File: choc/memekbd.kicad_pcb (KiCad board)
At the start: 2 copper layers, 3.6 x 3.1 mm, 192 parts, among them J1 USB_B_Micro, J2 USB_B_Micro, SW1 SW_Push, SW10 SW_Push, SW11 SW_Push, SW12 SW_Push, SW13 SW_Push, SW14 SW_Push, SW15 SW_Push, SW16 SW_Push, SW17 SW_Push, SW18 SW_Push, SW19 SW_Push, SW2 SW_Push, SW20 SW_Push, SW21 SW_Push, SW22 SW_Push, SW23 SW_Push, SW24 SW_Push, SW25 SW_Push, SW26 SW_Push, SW27 SW_Push, SW28 SW_Push, SW29 SW_Push, SW3 SW_Push, SW30 SW_Push, SW31 SW_Push, SW32 SW_Push, SW33 SW_Push, SW34 SW_Push, SW35 SW_Push, SW36 SW_Push, SW37 SW_Push, SW38 SW_Push, SW39 SW_Push, SW4 SW_Push, SW40 SW_Push, SW41 SW_Push, SW42 SW_Push, SW43 SW_Push, SW44 SW_Push, SW45 SW_Push, SW46 SW_Push, SW47 SW_Push, SW48 SW_Push, SW49 SW_Push, SW5 SW_Push, SW50 SW_Push, SW6 SW_Push, SW7 SW_Push, SW8 SW_Push, SW9 SW_Push, U1 ProMicro, U2 ProMicro

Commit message: work on choc version
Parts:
- moved H4 193.7 mm to (96.0, 21.8)
- moved H6 189.2 mm to (111.8, 96.5)
- moved H7 157.7 mm to (74.8, 96.5)
- moved H5 143.8 mm to (74.0, 21.8)
- moved H3 100.1 mm to (46.8, 73.5)
- moved C1 83.9 mm to (80.0, 104.5)
- moved C11 83.9 mm to (104.0, 104.5)
- moved C12 83.9 mm to (107.0, 104.5)
- moved C2 83.9 mm to (83.0, 104.5)
- moved C3 83.9 mm to (86.0, 104.5)
- moved C4 83.9 mm to (89.0, 104.5)
- moved C6 83.9 mm to (92.0, 104.5)
- moved C7 83.9 mm to (95.0, 104.5)
- moved C8 83.9 mm to (98.0, 104.5)
- moved C9 83.9 mm to (101.0, 104.5)
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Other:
- board size 3.6 x 3.1 mm -> 260 x 92.5 mm

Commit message: add mounting holes
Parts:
- moved H16 137.7 mm to (243.0, 73.2)
- moved H12 124.8 mm to (195.5, 21.5)
- moved H9 122.8 mm to (217.0, 21.5)
- moved H11 114.9 mm to (180.0, 96.0)
- moved H15 112.6 mm to (265.2, 28.5)
- moved H14 106.5 mm to (217.0, 96.0)
- moved H13 100.8 mm to (235.0, 89.2)
- moved H10 88.4 mm to (272.8, 87.8)
- moved H2 5.76 mm to (19.2, 88.2)
- moved H1 5.75 mm to (56.0, 89.8)
- moved C13 3.44 mm to (183.6, 106.2)
- moved C14 3.44 mm to (186.6, 106.2)
- moved C16 3.44 mm to (189.6, 106.2)
- moved C17 3.44 mm to (192.6, 106.2)
- moved C18 3.44 mm to (195.6, 106.2)
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
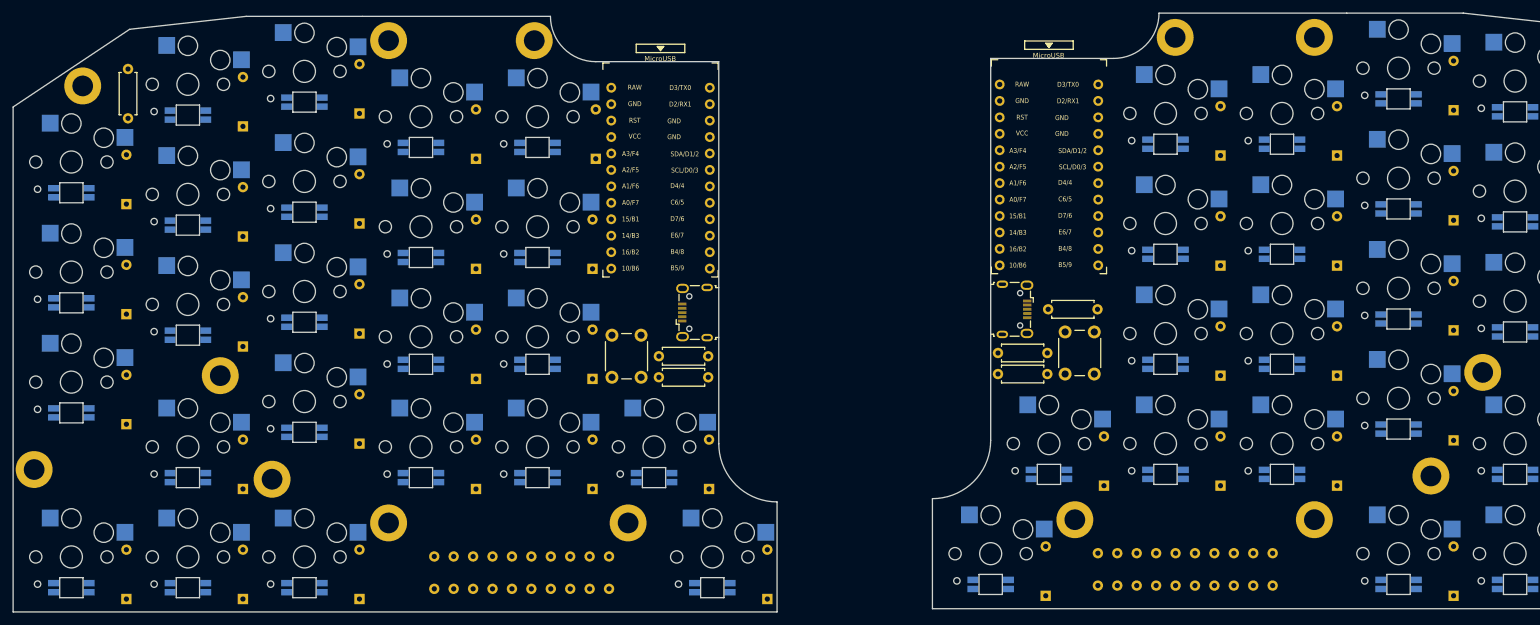
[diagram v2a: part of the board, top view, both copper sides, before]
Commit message: fix diodes not having vertical space in choc
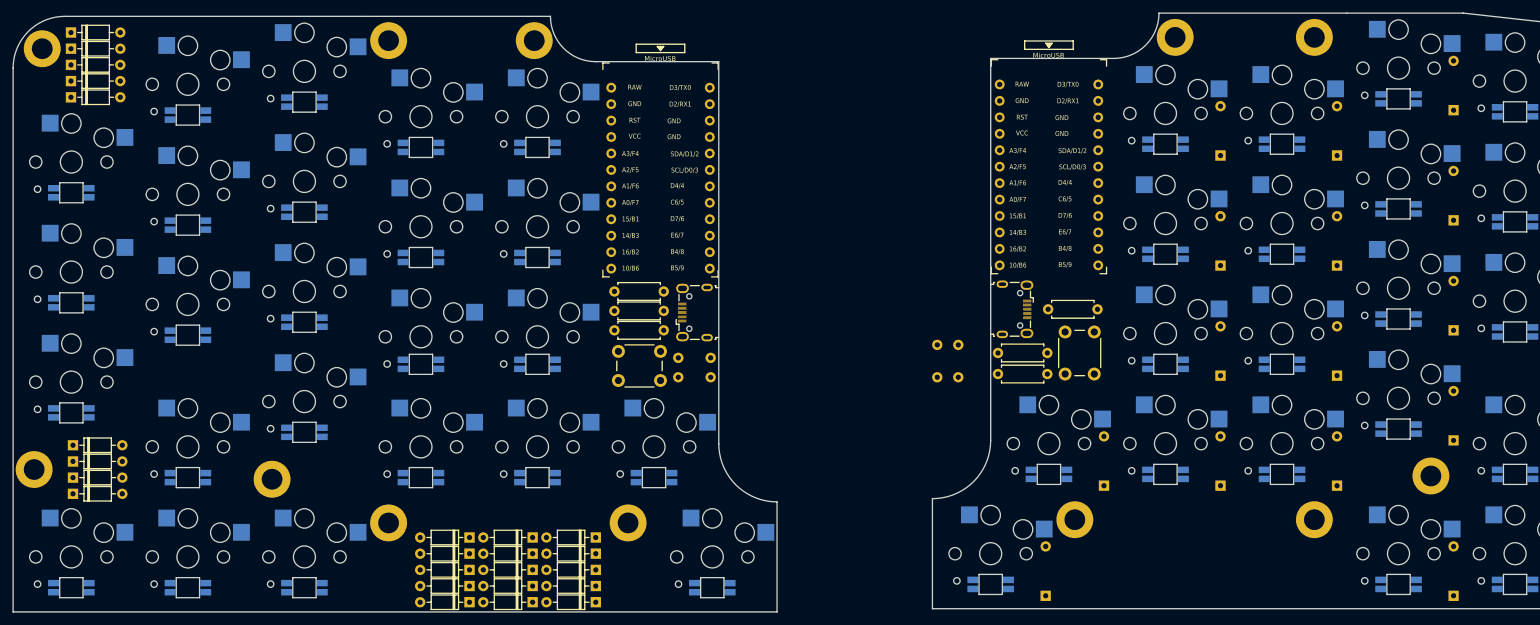
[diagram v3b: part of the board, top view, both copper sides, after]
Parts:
- removed C11, C12, C13, C14, C16, C17, C18, C19, C20, C21, C22, C23, C6, C7, C8, C9: 0.1uF, Capacitor_THT:C_Disc_D6.0mm_W2.5mm_P5.00mm
- removed H16, H3: MountingHole_Pad, MountingHole:MountingHole_3.2mm_M3_ISO7380_Pad
- D1, D10, D11, D12, D13, D14, D15, D16, D17, D18, D19, D2, D20, D21, D22, D23, D3, D4, D47, D5, D6, D7, D8, D9: moved to F.Cu
- moved R5 87.0 mm to (116.5, 60.8), turned to 180 degrees
- moved D20 83.4 mm to (24.9, 20.8), turned to 0 degrees
- moved C4 79.0 mm to (162.0, 74.0)
- moved C3 78.8 mm to (158.8, 74.0)
- moved D2 69.2 mm to (86.5, 108.8), turned to 180 degrees
- moved D3 68.5 mm to (96.2, 108.8), turned to 180 degrees
- moved D7 64.4 mm to (86.5, 106.2), turned to 180 degrees
- moved D16 63.3 mm to (24.9, 30.8), turned to 0 degrees
- moved D8 58.1 mm to (96.2, 106.2), turned to 180 degrees
- moved D12 56.1 mm to (86.5, 103.8), turned to 180 degrees
- moved C1 51.9 mm to (118.8, 71.0), turned to 0 degrees
- moved C2 47.7 mm to (118.8, 74.0), turned to 0 degrees
- moved D47 47.1 mm to (25.2, 92.0), turned to 0 degrees
- moved D21 45.6 mm to (86.5, 98.8), turned to 180 degrees
- moved D13 45.3 mm to (96.2, 103.8), turned to 180 degrees
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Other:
- outline, holes or cut-outs redrawn

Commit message: progress
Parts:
- moved H15 8.49 mm to (271.2, 22.5)
- moved H8 0.35 mm to (20.8, 23.0)
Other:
- outline, holes or cut-outs redrawn
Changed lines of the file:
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@@
     (pad "" np_thru_hole circle (at 5.5 0 180) (size 1.9 1.9) (drill 1.9) (layers F&B.Cu *.Mask))
     (pad "1" smd rect (at 3.275 6 180) (size 2.6 2.6) (layers "B.Cu" "B.Paste" "B.Mask")
-      (net 111 "/lcol4") (pinfunction "1") (pintype "passive"))
+      (net 111 "/lcol4") (pinfunction "1"))
     (pad "2" smd rect (at -8.275 3.8 180) (size 2.6 2.6) (layers "B.Cu" "B.Paste" "B.Mask")
-      (net 30 "Net-(D23-Pad2)") (pinfunction "2") (pintype "passive"))
+      (net 30 "Net-(D23-Pad2)") (pinfunction "2"))
   )
   (footprint "kbd:ChocV1_Hotswap" (layer "F.Cu")
@@
   )
   (footprint "MountingHole:MountingHole_3.2mm_M3_ISO7380_Pad" (layer "F.Cu")
-    (at 265.25 28.5)
+    (at 271.25 22.5)
     (descr "Mounting Hole 3.2mm, M3, ISO7380")
     (tags "mounting hole 3.2mm m3 iso7380")
@@
   )
   (footprint "MountingHole:MountingHole_3.2mm_M3_ISO7380_Pad" (layer "F.Cu")
-    (at 20.5 23.25)
+    (at 20.75 23)
     (descr "Mounting Hole 3.2mm, M3, ISO7380")
     (tags "mounting hole 3.2mm m3 iso7380")
@@
     )
   )
-  (gr_line (start 167 24.75) (end 167 83.75) (layer "Edge.Cuts") (width 0.05))
-  (gr_line (start 276 109.75) (end 276 31.75) (layer "Edge.Cuts") (width 0.05))
+  (gr_line (start 276 109.75) (end 276 25.75) (layer "Edge.Cuts") (width 0.05))
+  (gr_line (start 186 24.75) (end 167 24.75) (layer "Edge.Cuts") (width 0.05))
   (gr_arc (start 24 26.25) (end 16 26.25) (angle 90) (layer "Edge.Cuts") (width 0.05))
-  (gr_line (start 106 25.25) (end 125 25.25) (layer "Edge.Cuts") (width 0.05))
-  (gr_arc (start 134 84.25) (end 125 84.25) (angle -90) (layer "Edge.Cuts") (width 0.05))
-  (gr_line (start 240 17.75) (end 222 17.75) (layer "Edge.Cuts") (width 0.05))
   (gr_arc (start 158 83.75) (end 167 83.75) (angle 90) (layer "Edge.Cuts") (width 0.05))
   (gr_line (start 222 17.75) (end 193 17.75) (layer "Edge.Cuts") (width 0.05))
-  (gr_line (start 276 109.75) (end 158 109.75) (layer "Edge.Cuts") (width 0.05))
-  (gr_line (start 276 31.75) (end 258 19.75) (layer "Edge.Cuts") (width 0.05))
-  (gr_line (start 258 19.75) (end 240 17.75) (layer "Edge.Cuts") (width 0.05))
-  (gr_line (start 16 110.25) (end 134 110.25) (layer "Edge.Cuts") (width 0.05))
+  (gr_line (start 106 25.25) (end 125 25.25) (layer "Edge.Cuts") (width 0.05))
+  (gr_arc (start 134 84.25) (end 125 84.25) (angle -90) (layer "Edge.Cuts") (width 0.05))
   (gr_line (start 158 109.75) (end 158 92.75) (layer "Edge.Cuts") (width 0.05))
+  (gr_line (start 167 24.75) (end 167 83.75) (layer "Edge.Cuts") (width 0.05))
+  (gr_line (start 268 17.75) (end 222 17.75) (layer "Edge.Cuts") (width 0.05))
+  (gr_arc (start 186 17.75) (end 186 24.75) (angle -90) (layer "Edge.Cuts") (width 0.05))
+  (gr_arc (start 268 25.75) (end 276 25.75) (angle -90) (layer "Edge.Cuts") (width 0.05))
+  (gr_line (start 16 110.25) (end 134 110.25) (layer "Edge.Cuts") (width 0.05))
   (gr_line (start 24 18.25) (end 70 18.25) (layer "Edge.Cuts") (width 0.05))
-  (gr_line (start 186 24.75) (end 167 24.75) (layer "Edge.Cuts") (width 0.05))
   (gr_line (start 70 18.25) (end 99 18.25) (layer "Edge.Cuts") (width 0.05))
   (gr_line (start 125 25.25) (end 125 84.25) (layer "Edge.Cuts") (width 0.05))
   (gr_line (start 16 110.25) (end 16 26.25) (layer "Edge.Cuts") (width 0.05))
-  (gr_arc (start 186 17.75) (end 186 24.75) (angle -90) (layer "Edge.Cuts") (width 0.05))
+  (gr_line (start 276 109.75) (end 158 109.75) (layer "Edge.Cuts") (width 0.05))
   (gr_arc (start 106 18.25) (end 106 25.25) (angle 90) (layer "Edge.Cuts") (width 0.05))
   (gr_line (start 134 110.25) (end 134 93.25) (layer "Edge.Cuts") (width 0.05))

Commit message: progress
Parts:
- D24, D25, D26, D27, D28, D29, D30, D31, D32, D33, D34, D35, D36, D37, D38, D39, D40, D41, D42, D43, D44, D45, D46, D48: moved to F.Cu
- moved D45 84.4 mm to (194.8, 108.2), turned to 0 degrees
- moved D44 82.9 mm to (204.5, 108.2), turned to 0 degrees
- moved D40 75.0 mm to (204.5, 105.8), turned to 0 degrees
- moved D41 72.0 mm to (194.8, 105.8), turned to 0 degrees
- moved D24 66.2 mm to (265.8, 20.2), turned to 180 degrees
- moved D35 63.4 mm to (204.5, 103.2), turned to 0 degrees
- moved D46 58.8 mm to (185.0, 108.2), turned to 0 degrees
- moved D36 57.0 mm to (194.8, 103.2), turned to 0 degrees
- moved D29 48.3 mm to (265.8, 22.8), turned to 180 degrees
- moved D30 46.8 mm to (204.5, 100.8), turned to 0 degrees
- moved D25 41.5 mm to (204.5, 98.2), turned to 0 degrees
- moved D42 38.5 mm to (185.0, 105.8), turned to 0 degrees
- moved D31 37.3 mm to (194.8, 100.8), turned to 0 degrees
- moved D28 36.1 mm to (265.8, 84.0), turned to 180 degrees
- moved D34 28.3 mm to (265.8, 25.2), turned to 180 degrees
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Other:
- board size 260 x 92.5 mm -> 259 x 92.5 mm

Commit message: progress on plates
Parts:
- added H1: MountingHole_Pad, MountingHole:MountingHole_3.2mm_M3_ISO7380_Pad, F.Cu at (207.0, 195.5)
- added H1: MountingHole_Pad, MountingHole:MountingHole_3.2mm_M3_ISO7380_Pad, F.Cu at (60.5, 192.5)
- added H2: MountingHole_Pad, MountingHole:MountingHole_3.2mm_M3_ISO7380_Pad, F.Cu at (24.5, 191.0)
- added H2: MountingHole_Pad, MountingHole:MountingHole_3.2mm_M3_ISO7380_Pad, F.Cu at (171.0, 194.0)
- added H4: MountingHole_Pad, MountingHole:MountingHole_3.2mm_M3_ISO7380_Pad, F.Cu at (248.2, 127.8)
- added H4: MountingHole_Pad, MountingHole:MountingHole_3.2mm_M3_ISO7380_Pad, F.Cu at (101.8, 124.8)
- added H5: MountingHole_Pad, MountingHole:MountingHole_3.2mm_M3_ISO7380_Pad, F.Cu at (225.0, 127.8)
- added H5: MountingHole_Pad, MountingHole:MountingHole_3.2mm_M3_ISO7380_Pad, F.Cu at (78.5, 124.8)
- added H6: MountingHole_Pad, MountingHole:MountingHole_3.2mm_M3_ISO7380_Pad, F.Cu at (117.0, 199.2)
- added H6: MountingHole_Pad, MountingHole:MountingHole_3.2mm_M3_ISO7380_Pad, F.Cu at (263.5, 202.2)
- added H7: MountingHole_Pad, MountingHole:MountingHole_3.2mm_M3_ISO7380_Pad, F.Cu at (78.5, 199.2)
- added H7: MountingHole_Pad, MountingHole:MountingHole_3.2mm_M3_ISO7380_Pad, F.Cu at (225.0, 202.2)
- added H8: MountingHole_Pad, MountingHole:MountingHole_3.2mm_M3_ISO7380_Pad, F.Cu at (172.5, 128.8)
- added H8: MountingHole_Pad, MountingHole:MountingHole_3.2mm_M3_ISO7380_Pad, F.Cu at (26.0, 125.8)
- added SW2: KEY_SWITCH, kbd:ChocV1_Hole, F.Cu at (176.8, 163.5)
- added SW2: KEY_SWITCH, kbd:ChocV1_Hole, F.Cu at (248.8, 139.5)
- added SW2: KEY_SWITCH, kbd:ChocV1_Hole, F.Cu at (194.8, 190.5)
- added SW2: KEY_SWITCH, kbd:ChocV1_Hole, F.Cu at (248.8, 190.5)
- added SW2: KEY_SWITCH, kbd:ChocV1_Hole, F.Cu at (176.8, 146.5)
- added SW2: KEY_SWITCH, kbd:ChocV1_Hole, F.Cu at (194.8, 168.5)
- added SW2: KEY_SWITCH, kbd:ChocV1_Hole, F.Cu at (266.8, 190.5)
- added SW2: KEY_SWITCH, kbd:ChocV1_Hole, F.Cu at (275.8, 207.5)
- added SW2: KEY_SWITCH, kbd:ChocV1_Hole, F.Cu at (194.8, 151.5)
- added SW2: KEY_SWITCH, kbd:ChocV1_Hole, F.Cu at (212.8, 149.5)
- added SW2: KEY_SWITCH, kbd:ChocV1_Hole, F.Cu at (176.8, 207.5)
- added SW2: KEY_SWITCH, kbd:ChocV1_Hole, F.Cu at (194.8, 134.5)
- added SW2: KEY_SWITCH, kbd:ChocV1_Hole, F.Cu at (194.8, 207.5)
- added SW2: KEY_SWITCH, kbd:ChocV1_Hole, F.Cu at (230.8, 139.5)
- added SW2 (x2): KEY_SWITCH, kbd:ChocV1_Hole, F.Cu at (212.8, 207.5)
- added SW2: KEY_SWITCH, kbd:ChocV1_Hole, F.Cu at (248.8, 173.5)
- added SW2: KEY_SWITCH, kbd:ChocV1_Hole, F.Cu at (212.8, 183.5)
- added SW2: KEY_SWITCH, kbd:ChocV1_Hole, F.Cu at (248.8, 156.5)
- added SW2: KEY_SWITCH, kbd:ChocV1_Hole, F.Cu at (230.8, 173.5)
- added SW2: KEY_SWITCH, kbd:ChocV1_Hole, F.Cu at (230.8, 190.5)
- added SW2: KEY_SWITCH, kbd:ChocV1_Hole, F.Cu at (212.8, 132.5)
- added SW2: KEY_SWITCH, kbd:ChocV1_Hole, F.Cu at (212.8, 166.5)
- added SW2: KEY_SWITCH, kbd:ChocV1_Hole, F.Cu at (230.8, 156.5)
- added SW2: KEY_SWITCH, kbd:ChocV1_Hole, F.Cu at (176.8, 180.5)
- moved D12 2.00 mm to (86.5, 101.8)
- moved D13 2.00 mm to (96.2, 101.8)
- moved D14 2.00 mm to (106.0, 101.8)
- moved D17 2.00 mm to (86.5, 99.2)
- moved D18 2.00 mm to (96.2, 99.2)
- moved D19 2.00 mm to (106.0, 99.2)
- moved D2 2.00 mm to (86.5, 106.8)
- moved D21 2.00 mm to (86.5, 96.8)
- moved D22 2.00 mm to (96.2, 96.8)
- moved D23 2.00 mm to (106.0, 96.8)
- moved D25 2.00 mm to (204.5, 96.2)
- moved D26 2.00 mm to (194.8, 96.2)
- moved D27 2.00 mm to (185.0, 96.2)
- moved D3 2.00 mm to (96.2, 106.8)
- moved D30 2.00 mm to (204.5, 98.8)
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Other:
- board size 259 x 92.5 mm -> 268.8 x 198.2 mm

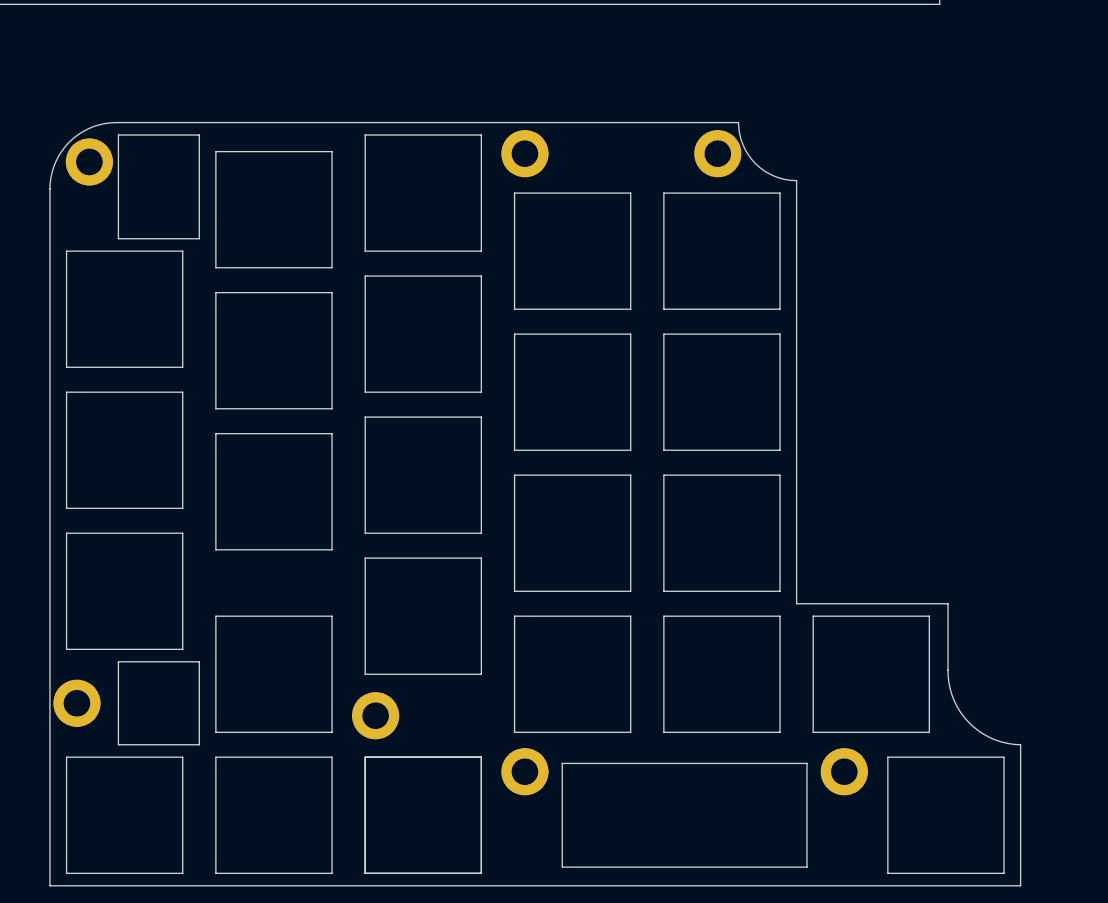
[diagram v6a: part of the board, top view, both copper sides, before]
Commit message: add routed left board
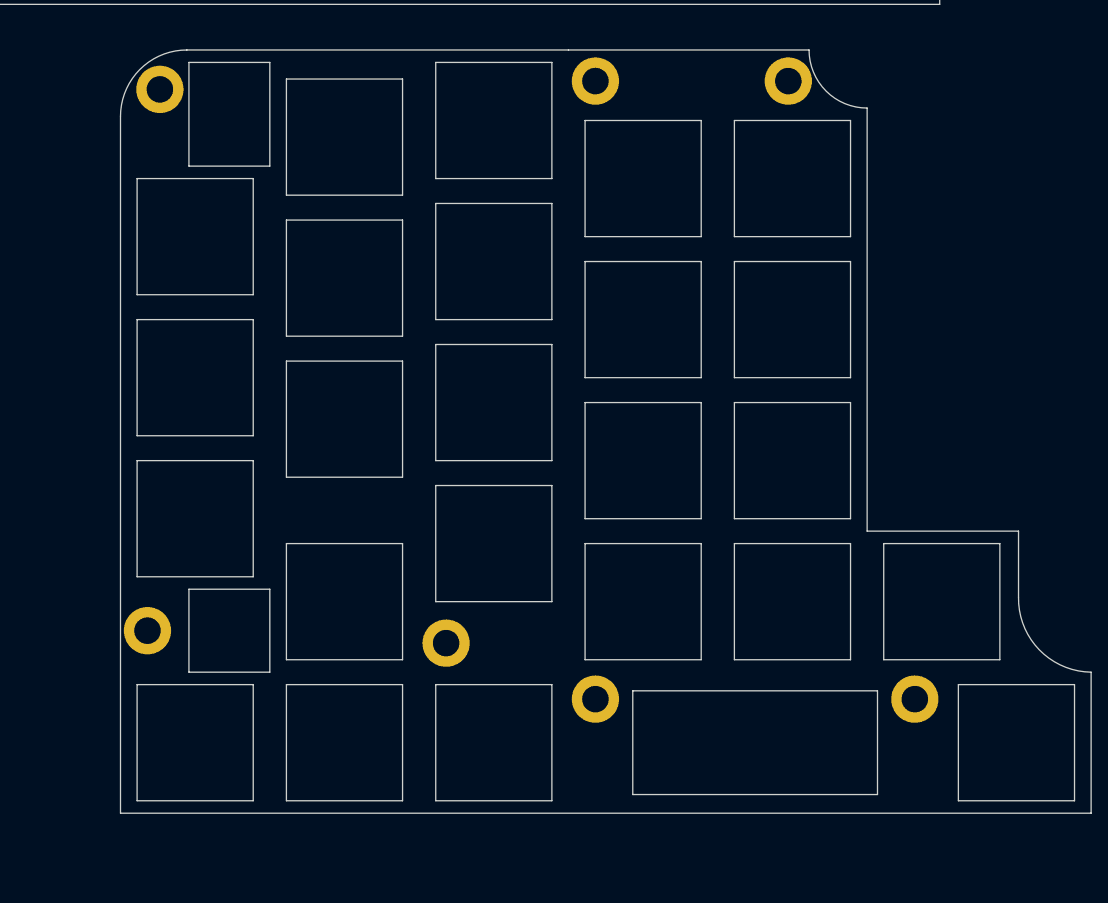
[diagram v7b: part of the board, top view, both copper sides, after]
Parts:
- removed the SW2 at (212.8, 207.5)
- moved REF** 12.2 mm to (185.2, 198.8)
- moved REF** 12.2 mm to (185.2, 171.8)
- moved REF** 12.2 mm to (185.2, 154.8)
- moved REF** 12.2 mm to (257.2, 130.8)
- moved REF** 12.2 mm to (256.8, 119.0)
- moved REF** 12.2 mm to (203.2, 181.8)
- moved REF** 12.2 mm to (257.2, 181.8)
- moved REF** 12.2 mm to (233.5, 119.0)
- moved REF** 12.2 mm to (185.2, 137.8)
- moved REF** 12.2 mm to (215.5, 186.8)
- moved REF** 12.2 mm to (181.0, 120.0)
- moved REF** 12.2 mm to (203.2, 159.8)
- moved REF** 12.2 mm to (233.5, 193.5)
- moved REF** 12.2 mm to (179.5, 185.2)
- moved REF** 12.2 mm to (275.2, 181.8)
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- renumbered SW2 to REF**, H7 to REF**, H4 to REF**, H6 to REF**, H5 to REF**, H1 to REF**, H8 to REF**, H2 to REF**
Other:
- board size 268.8 x 198.2 mm -> 277.2 x 195.2 mm
